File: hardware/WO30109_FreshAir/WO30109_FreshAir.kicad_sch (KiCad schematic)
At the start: 76 parts, among them J5 DI 12V/IN1-4/COM/GND, K1 G5Q-1 DC12, K2 G5Q-1 DC12, K3 G5Q-1 DC12, K4 G5Q-1 DC12, P1 AC IN 230V, P2 PROG, P3 AC OUT, Q1 Si2302CDS, Q2 Si2302CDS, Q3 Si2302CDS, Q4 Si2302CDS, U1 ESP32-C6-WROOM-1-N8, U2 IRM-02-12, U3 SYN480R, U4 AP63203WU-7, U5 TLP290-4, U6 ST25DV04KC-IE6S3, Y1 13.52127MHz 20pF

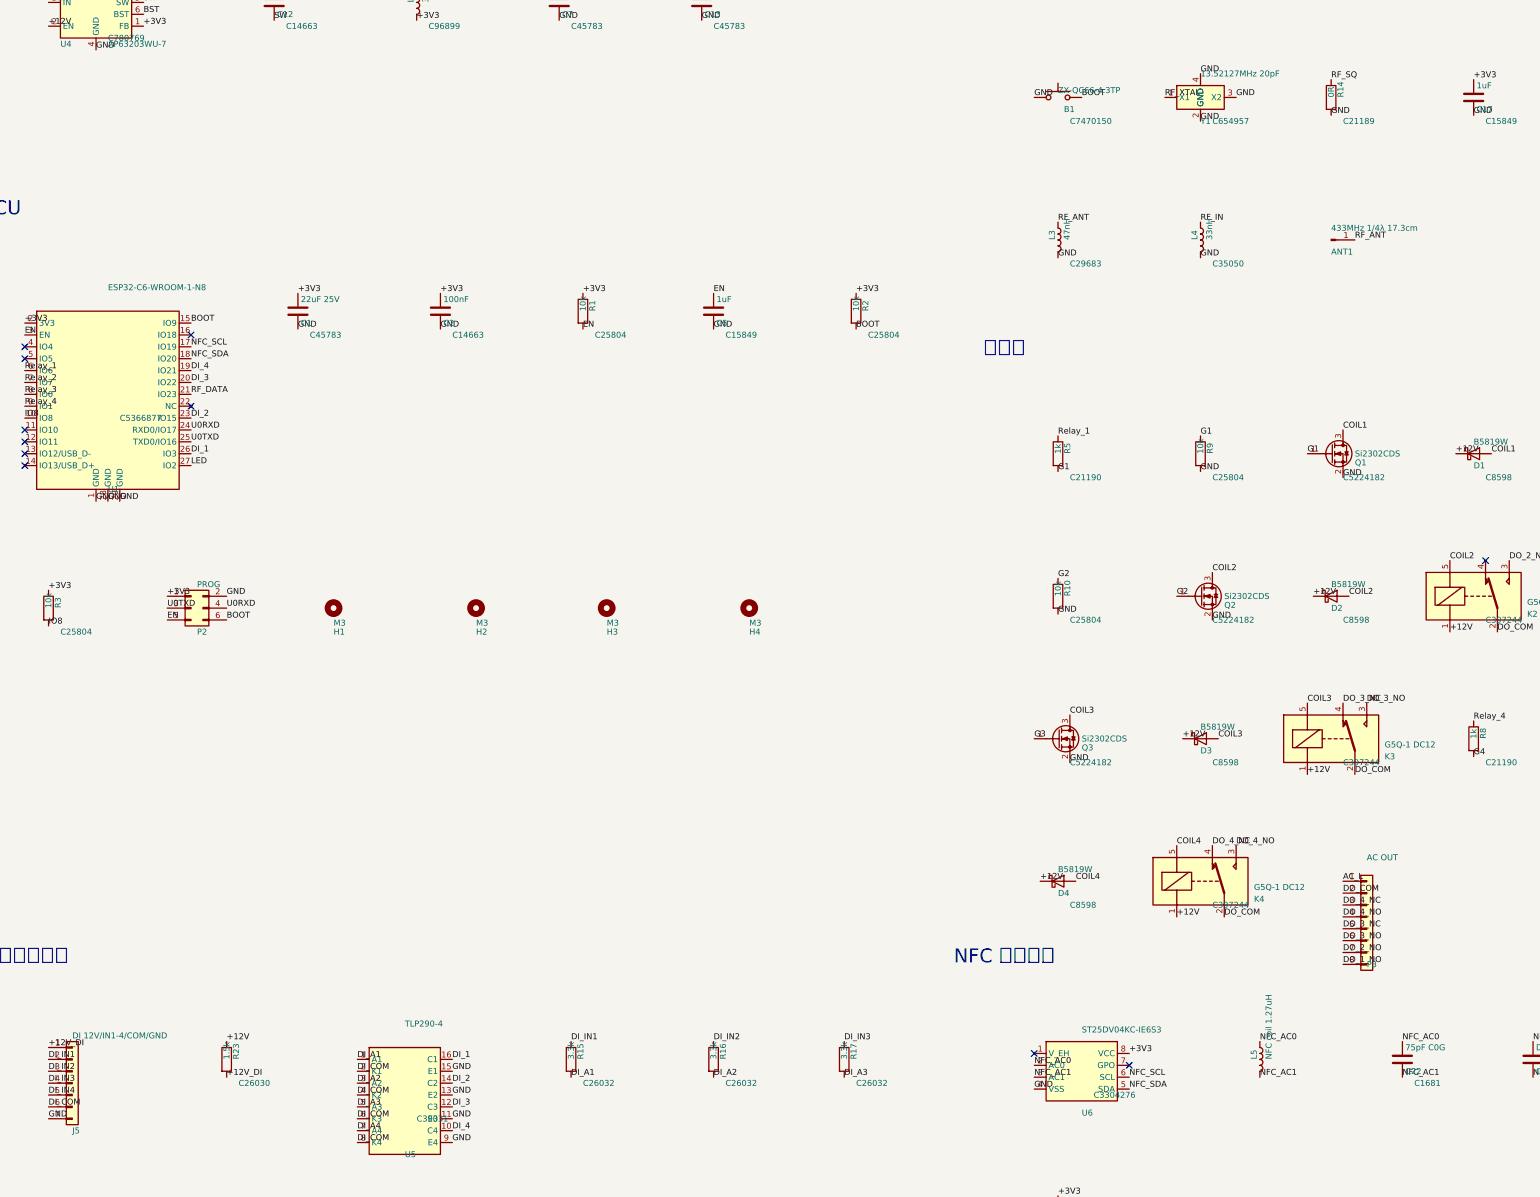
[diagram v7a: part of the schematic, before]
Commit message: hw: V3.4 照外殼 4-02-3 放回原板框（DI 2.54mm、NFC 外接 FPC 天線）
外殼是精鋼塑模 4-02-3（35mm 導軌盒 88×72×59，螺絲 50×50）；原板 63.4×83.08 本來就是照它做的。
V3.2／V3.3 加高的板子放不進外殼，V3.3 的板上 NFC 線圈離前蓋 >50mm 讀不到。

- J5 改 KF2EDGR-2.54-7P（C577599），和 P1 共用上方開窗，焊盤離市電 9.08mm
- NFC 板上線圈拿掉，J6（JST SH 2P，C160388）接 FPC 天線；C22/C24 依天線電感調諧（不上件）
- P2 改背面 2×3 燒錄測試點；B1 改 TS-1088（C720477 基礎料）放 J5 後方
- build_v34.sh：從 V3.1 換件擺件，低壓全部 Freerouting 重佈（第一輪即 0 未連線）
- mains_router.board_height() 不再把板邊線寬算進去（格點偏 0.05mm）
- ERC 0；DRC 錯誤 0、未連線 0、parity 0；CPL J6 以 JLC 封裝改正為 180°

Co-Authored-By: Claude Opus 5.5 (1M context) <noreply@anthropic.com>
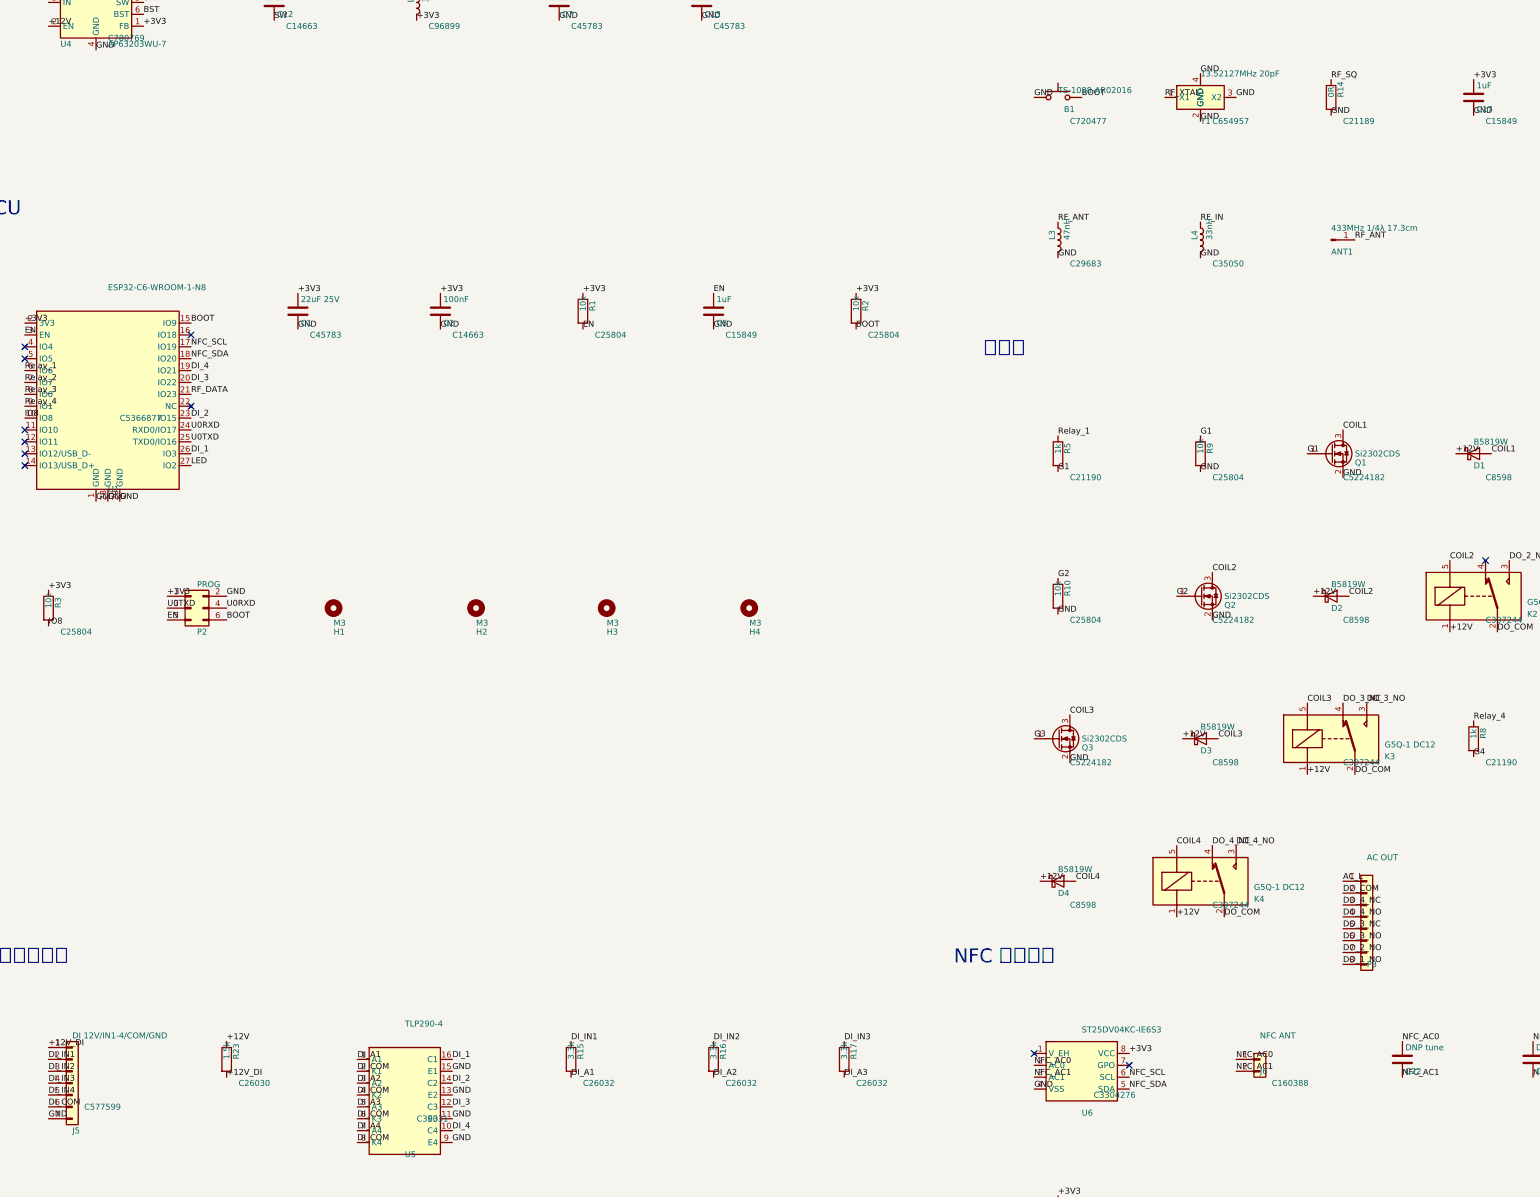
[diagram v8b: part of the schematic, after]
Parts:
- removed L5: NFC coil 1.27uH, WOOW:NFC_Coil_14.9x14.6mm_8T, symbol Device:L
- added J6: NFC ANT, Connector_JST:JST_SH_BM02B-SRSS-TB_1x02-1MP_P1.00mm_Vertical, symbol Connector_Generic:Conn_01x02
- B1: value ZX-QC66-4.3TP -> TS-1088-AR02016; footprint WOOW:SW_Push_6x6mm_SMD_ZX-QC66 -> WOOW:SW_SPST_TS-1088; LCSC C7470150 -> C720477
- C22: value 75pF C0G -> DNP tune; LCSC C1681 -> (none); now left out of the parts list
- J5: footprint WOOW:TerminalBlock_Pluggable_1x07_P3.50mm_Horizontal -> WOOW:TerminalBlock_Pluggable_1x07_P2.54mm_Horizontal; LCSC (none) -> C577599
- P2: footprint Connector_PinHeader_2.54mm:PinHeader_2x03_P2.54mm_Vertical -> WOOW:ProgPads_2x03_P2.54mm; now left out of the parts list
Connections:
- net NFC_AC0: now also J6.1 (Pin_1)
- net NFC_AC1: now also J6.2 (Pin_2)
